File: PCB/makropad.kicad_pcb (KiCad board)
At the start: 2 copper layers, 82 x 85 mm, 53 parts, among them J1 OLED_DISPLAY, J2 Conn_01x04, J3 Conn_01x04, J4 Conn_01x04, J5 Conn_01x04, SW1 SW_Push_45deg, SW10 SW_Push_45deg, SW11 RotaryEncoder_Switch, SW12 RotaryEncoder_Switch, SW2 SW_Push_45deg, SW3 SW_Push_45deg, SW4 SW_Push_45deg, SW5 SW_Push_45deg, SW6 SW_Push_45deg, SW7 SW_Push_45deg, SW8 SW_Push_45deg, SW9 SW_Push_45deg, U1 PCF8574A, U2 MOUDLE-SEEEDUINO-XIAO

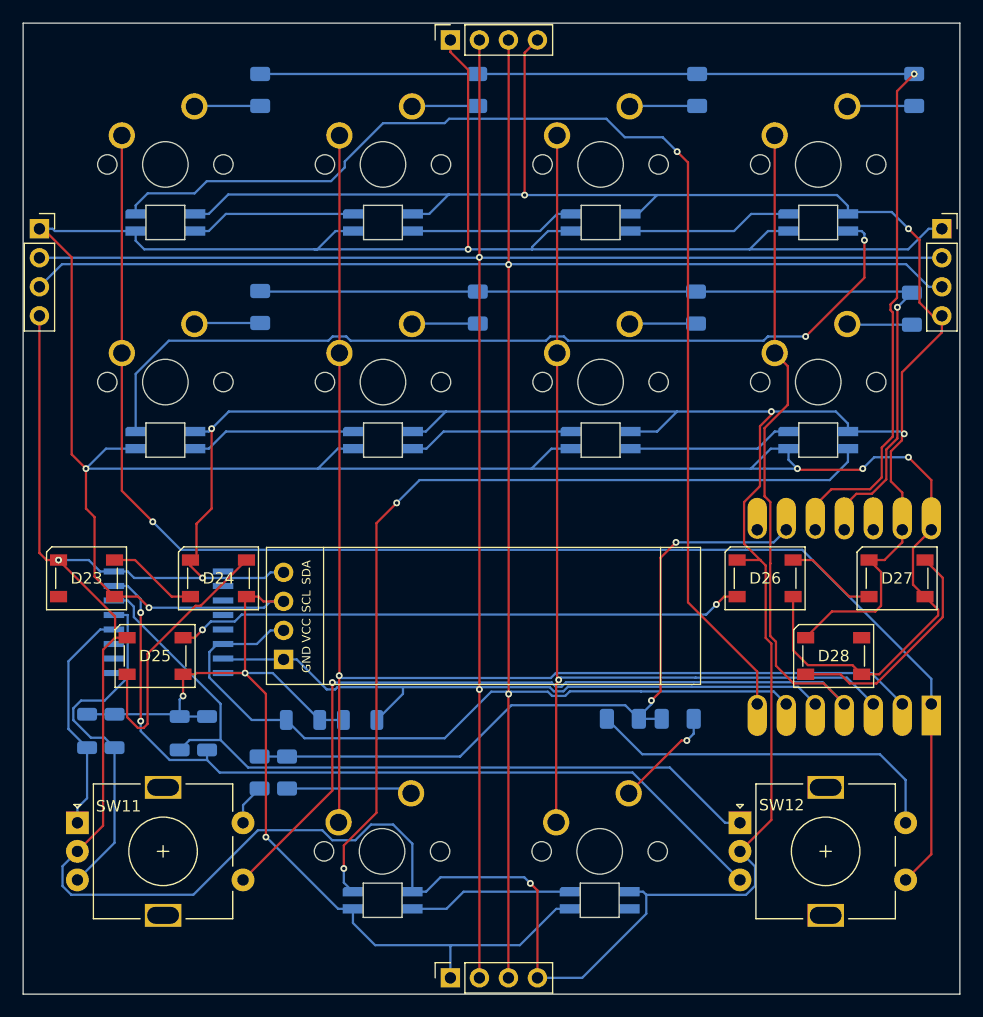
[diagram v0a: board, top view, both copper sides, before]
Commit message: feat: switch to SOD-123 diodes
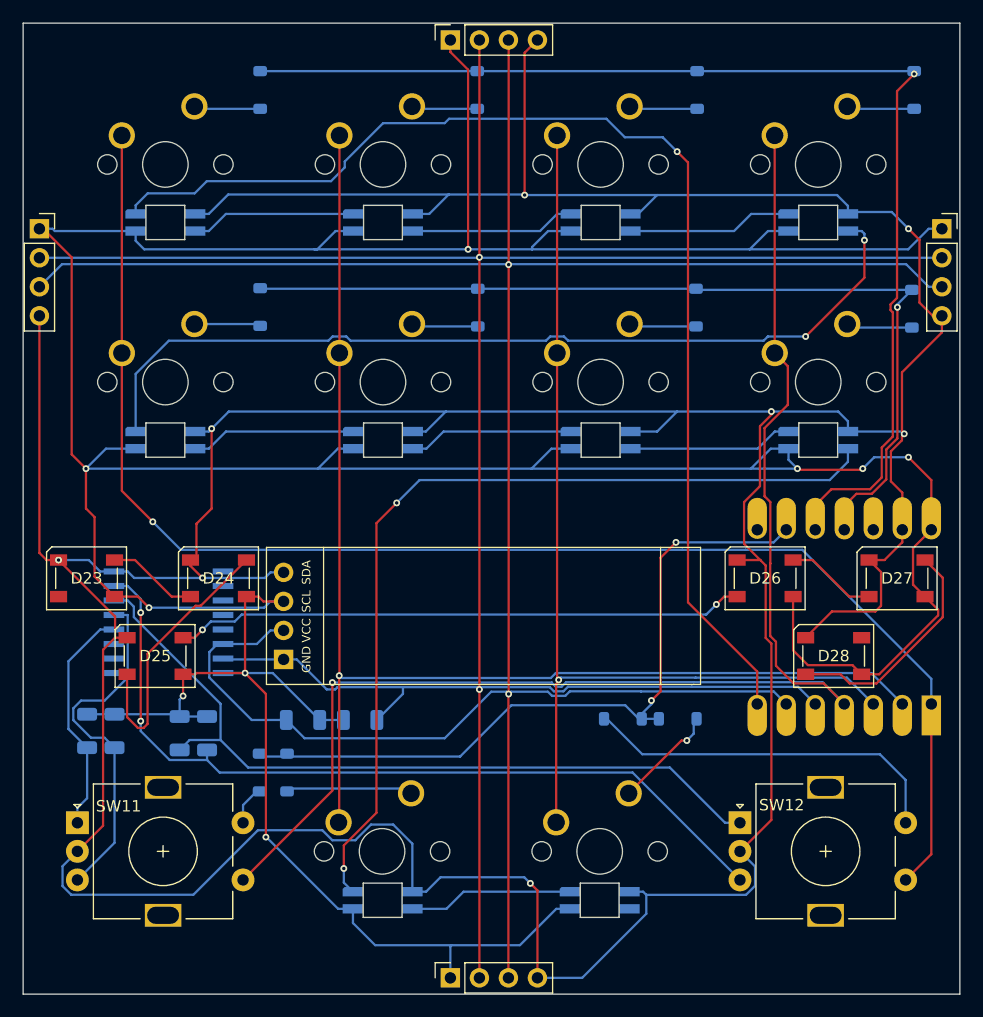
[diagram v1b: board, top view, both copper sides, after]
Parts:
- D1, D10, D11, D12, D2, D3, D4, D5, D6, D7, D8, D9: footprint Diode_SMD:D_1206_3216Metric -> Diode_SMD:D_SOD-123
